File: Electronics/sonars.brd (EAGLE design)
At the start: 74.6 x 59.7 mm, 6 parts, among them X1 GLX-S-88M

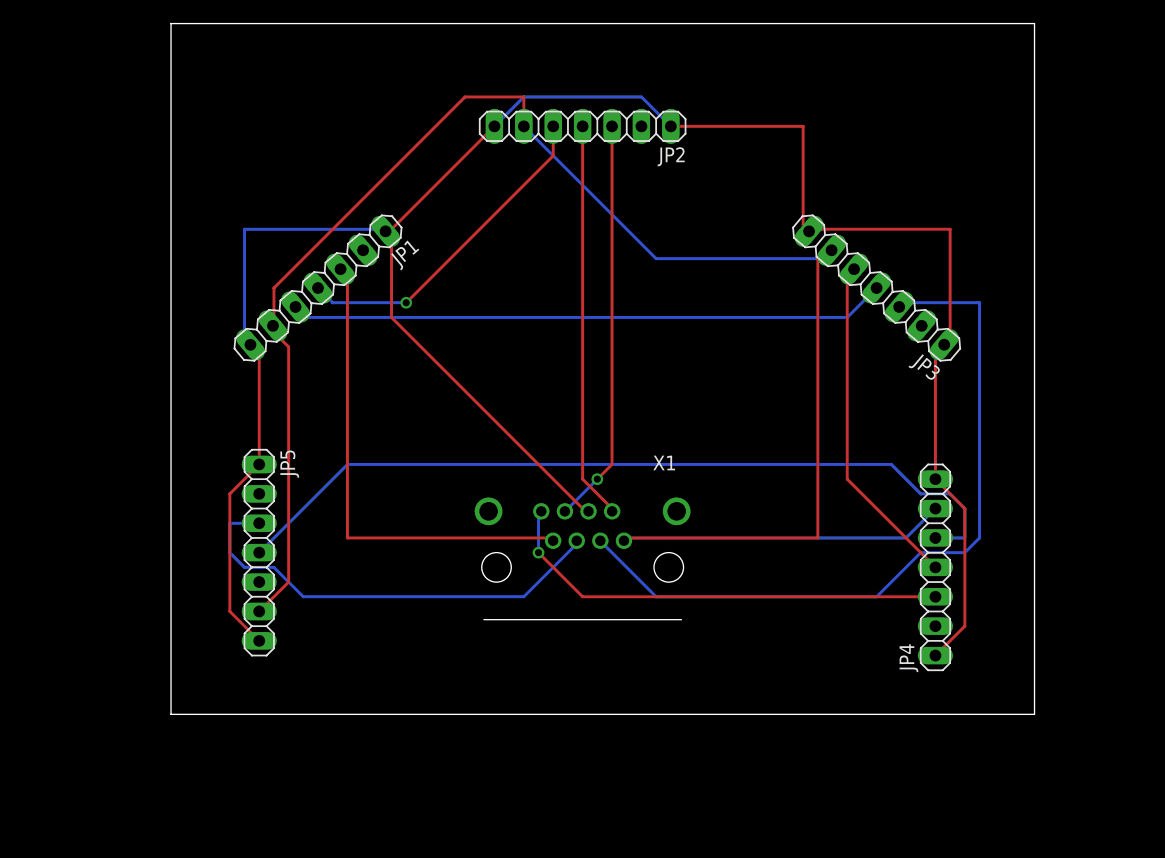
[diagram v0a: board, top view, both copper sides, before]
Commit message: Parts match physical size
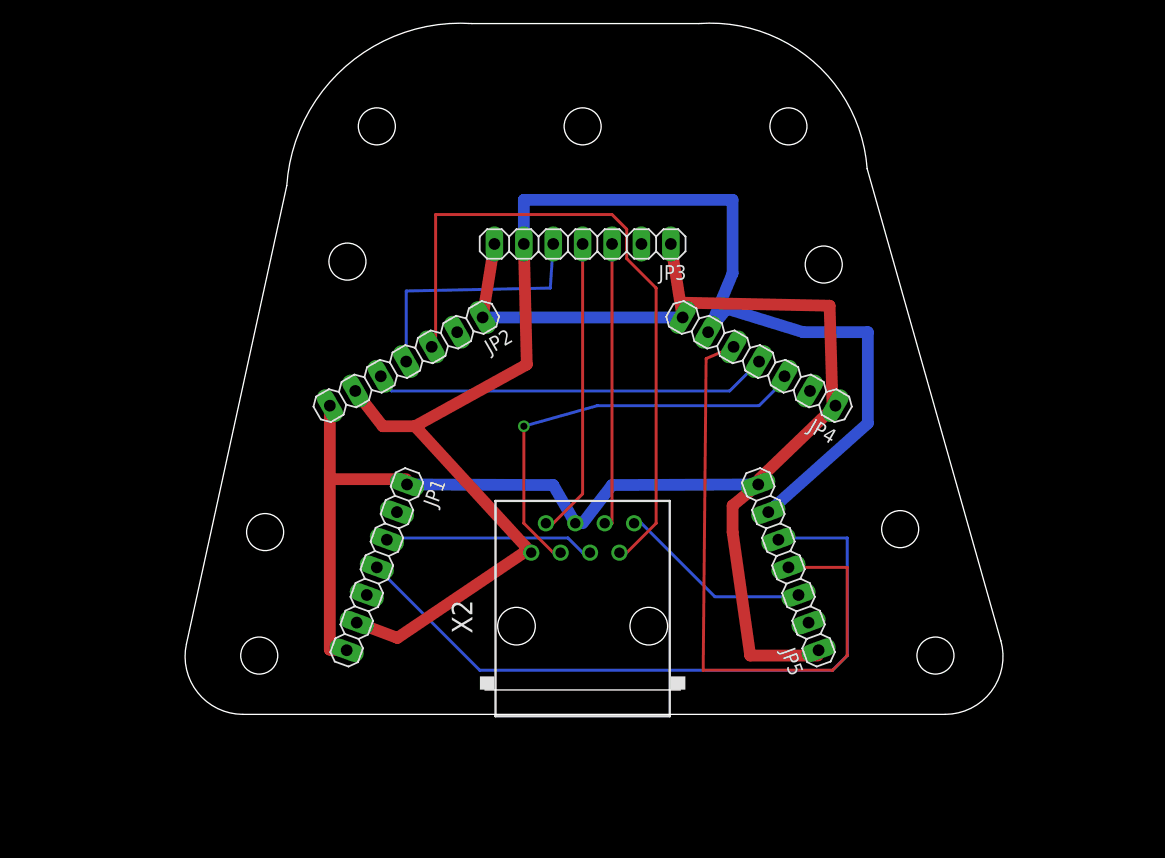
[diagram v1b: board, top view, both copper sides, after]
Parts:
- removed X1: GLX-S-88M, con-kycon:GLX-S-88M
- added X2: RJ45-8L-B, con-tycoelectronics:RJ45-NO-SHIELD
- JP1: value (none) -> Left
- JP2: value (none) -> Front left
- JP3: value (none) -> Front
- JP4: value (none) -> Front right
- JP5: value (none) -> Right
- moved JP5 45.7 mm to (66.0, 22.9), turned to 110 degrees
- moved JP3 25.7 mm to (48.3, 50.8), turned to 180 degrees
- moved JP2 25.4 mm to (33.0, 40.6), turned to 210 degrees
- moved JP1 24.7 mm to (30.5, 22.9), turned to 250 degrees
- moved JP4 23.4 mm to (63.5, 40.6), turned to 150 degrees
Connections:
- net N$10 renamed FR>R
- removed net N$1: JP2.3, X1.6
- removed net N$11: JP4.3, X1.8
- removed net N$12: JP5.3, X1.5
- removed net N$2: JP1.3, X1.7
- removed net N$3: JP3.3, X1.3
- removed net N$5: JP2.4, X1.2
- removed net N$7: JP1.4, JP2.5
- removed net N$8: JP1.5, JP3.4
- removed net N$9: JP3.5, JP4.4
- new net CHN: JP3.4, X2.2
- new net F: JP3.3, X2.6
- new net F>FL: JP2.4, JP3.5
- new net FL: JP2.3, X2.7
- new net FL>FR: JP2.5, JP4.4
- new net FR: JP4.3, X2.3
- new net L: JP1.3, X2.5
- new net R: JP5.3, X2.8
- new net R>L: JP1.4, JP5.5
- net +5V: now also X2.1; no longer X1.1
- net GND: now also X2.4; no longer X1.4
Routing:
- net N$3: track 64.9 -> 0.00 mm
- net R>L: track 0.00 -> 61.0 mm
- net FL: track 0.00 -> 59.5 mm
- net N$8: track 51.7 -> 0.00 mm
- net N$2: track 41.6 -> 0.00 mm
- net N$11: track 40.0 -> 0.00 mm, vias 1 -> 0
- net N$12: track 39.8 -> 0.00 mm
- net FR: track 0.00 -> 37.1 mm, vias 0 -> 1
- net N$1: track 35.0 -> 0.00 mm, vias 1 -> 0
- net FL>FR: track 0.00 -> 34.9 mm
- net N$5: track 34.3 -> 0.00 mm
- net +5V: track 162.5 -> 129.8 mm
- net GND: track 185.2 -> 153.5 mm
- net N$9: track 29.3 -> 0.00 mm
- net N$7: track 28.6 -> 0.00 mm, vias 1 -> 0
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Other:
- board size 74.6 x 59.7 mm -> 70.7 x 59.7 mm

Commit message: Rear facing sonars; angles adjusted
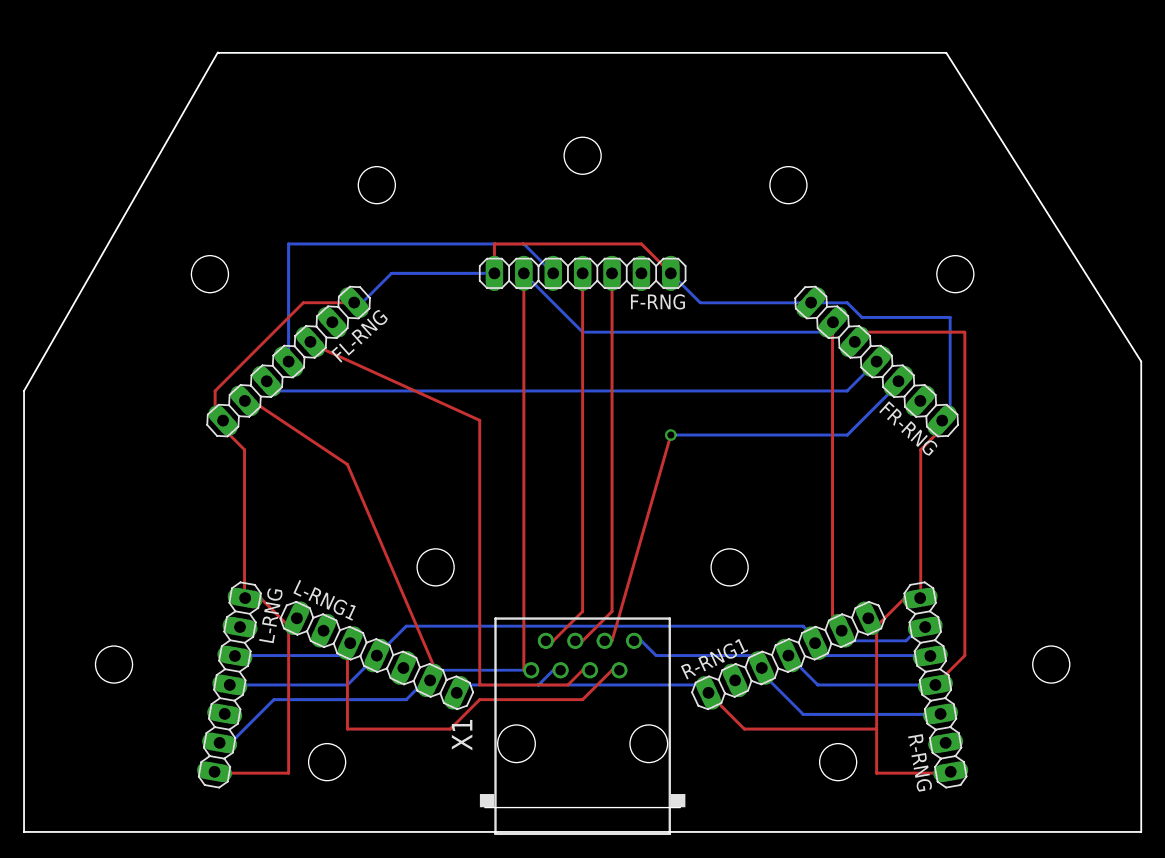
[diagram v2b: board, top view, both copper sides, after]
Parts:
- removed JP1: Left, pinhead:1X07
- removed JP2: Front left, pinhead:1X07
- removed JP3: Front, pinhead:1X07
- removed JP4: Front right, pinhead:1X07
- removed JP5: Right, pinhead:1X07
- removed X2: RJ45-8L-B, con-tycoelectronics:RJ45-NO-SHIELD
- added F-RNG: Front, pinhead:1X07
- added FL-RNG: Front left, pinhead:1X07
- added FR-RNG: Front right, pinhead:1X07
- added L-RNG: Left, pinhead:1X07
- added L-RNG1: Back Left, pinhead:1X07
- added R-RNG: Right, pinhead:1X07
- added R-RNG1: Back, pinhead:1X07
- added X1: RJ45-8L-B, con-tycoelectronics:RJ45-NO-SHIELD
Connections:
- removed net F: JP3.3, X2.6
- removed net FL: JP2.3, X2.7
- removed net FR: JP4.3, X2.3
- removed net L: JP1.3, X2.5
- removed net R: JP5.3, X2.8
- new net FL_RNG: FL-RNG.3, X1.5
- new net FR_RNG: FR-RNG.3, X1.6
- new net F_RNG: F-RNG.3, X1.4
- new net L_RNG: L-RNG.3, L-RNG1.3, X1.7
- new net R_RNG: R-RNG.3, R-RNG1.3, X1.8
- net +5V: now also F-RNG.6, FL-RNG.6, FR-RNG.6, L-RNG.6, L-RNG1.6, R-RNG.6, R-RNG1.6, X1.1; no longer JP1.6, JP2.6, JP3.6, JP4.6, JP5.6, X2.1
- net CHN: now also F-RNG.4, X1.2; no longer JP3.4, X2.2
- net F>FL: now also F-RNG.5, FL-RNG.4; no longer JP2.4, JP3.5
- net FL>FR: now also FL-RNG.5, FR-RNG.4; no longer JP2.5, JP4.4
- net FR>R: now also FR-RNG.5, R-RNG.4, R-RNG1.4; no longer JP4.5, JP5.4
- net GND: now also F-RNG.1, F-RNG.7, FL-RNG.1, FL-RNG.7, FR-RNG.1, FR-RNG.7, L-RNG.1, L-RNG.7, L-RNG1.1, L-RNG1.7, R-RNG.1, R-RNG.7, R-RNG1.1, R-RNG1.7, X1.3; no longer JP1.1, JP1.7, JP2.1, JP2.7, JP3.1, JP3.7, JP4.1, JP4.7, JP5.1, JP5.7, X2.4
- net R>L: now also L-RNG.4, L-RNG1.4, R-RNG.5, R-RNG1.5; no longer JP1.4, JP5.5
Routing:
- net FL: track 59.5 -> 0.00 mm
- net GND: track 153.5 -> 208.2 mm
- net FL_RNG: track 0.00 -> 49.0 mm
- net L_RNG: track 0.00 -> 43.9 mm
- net FR_RNG: track 0.00 -> 40.8 mm, vias 0 -> 1
- net FR: track 37.1 -> 0.00 mm, vias 1 -> 0
- net F_RNG: track 0.00 -> 33.4 mm
- net +5V: track 129.8 -> 160.4 mm
- net R_RNG: track 0.00 -> 30.0 mm
- net F: track 24.8 -> 0.00 mm
- net FL>FR: track 34.9 -> 54.2 mm
- net L: track 18.1 -> 0.00 mm
- net R: track 16.8 -> 0.00 mm
- net F>FL: track 22.4 -> 34.1 mm
- net CHN: track 25.8 -> 33.4 mm
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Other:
- board size 70.7 x 59.7 mm -> 96.5 x 67.3 mm

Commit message: Silkscreens; smaller sonar board
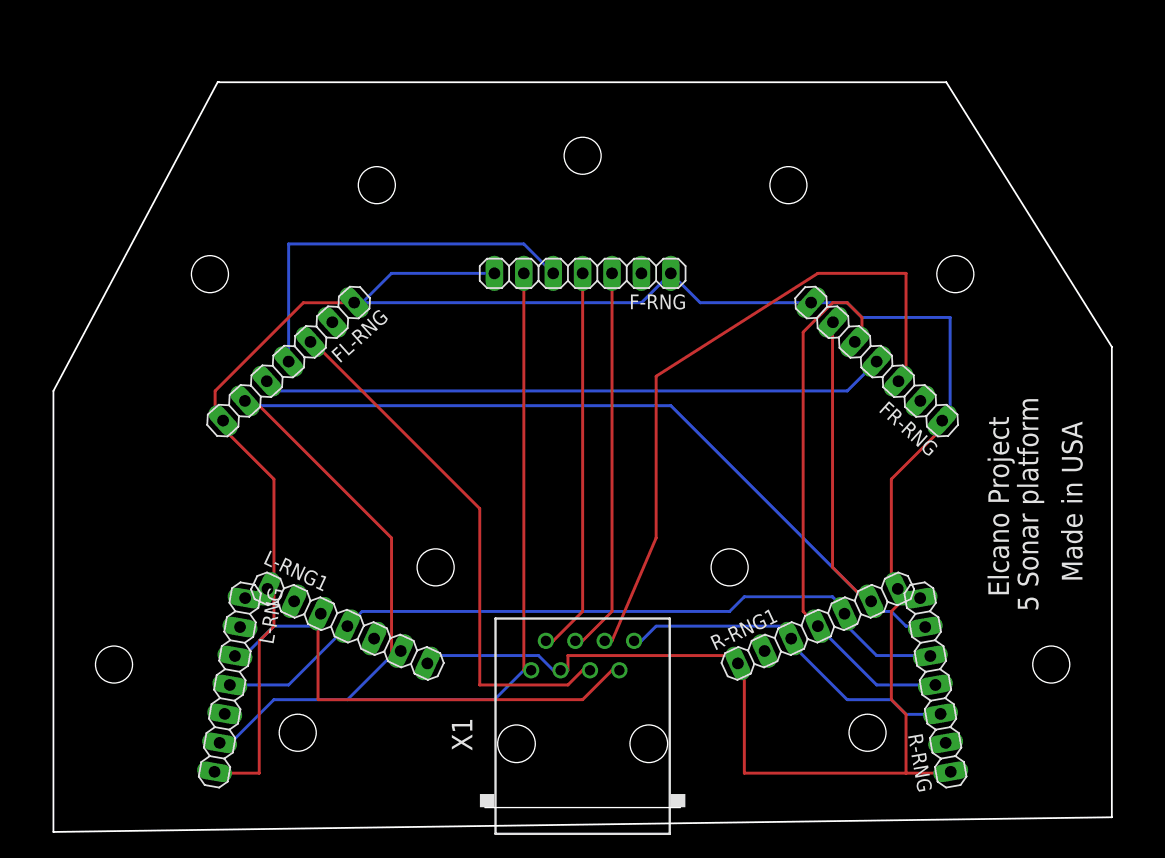
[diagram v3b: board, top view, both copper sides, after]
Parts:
- L-RNG1: value Back Left -> Back Left
- R-RNG1: value Back -> Back Right
- moved L-RNG1 3.59 mm to (27.9, 17.8)
- moved R-RNG1 3.59 mm to (68.6, 17.8)
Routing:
- net +5V: track 160.4 -> 191.7 mm
- net GND: track 208.2 -> 226.0 mm
- net FR_RNG: track 40.8 -> 58.1 mm, vias 1 -> 0
- net FR>R: track 55.2 -> 47.2 mm
- net FL_RNG: track 49.0 -> 45.8 mm
- net R>L: track 64.6 -> 66.7 mm
- net R_RNG: track 30.0 -> 31.0 mm
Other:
- board size 96.5 x 67.3 mm -> 91.4 x 64.8 mm
- board text added: "5 Sonar platform"
- board text added: "Elcano Project"
- board text added: "Made in USA"
